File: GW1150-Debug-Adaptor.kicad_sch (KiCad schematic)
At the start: 5 parts, among them J1 SW_SPDT, J2 Conn_02x03_Counter_Clockwise, J3 Conn_02x03_Counter_Clockwise, J4 SW_SPDT, J5 Conn_01x06

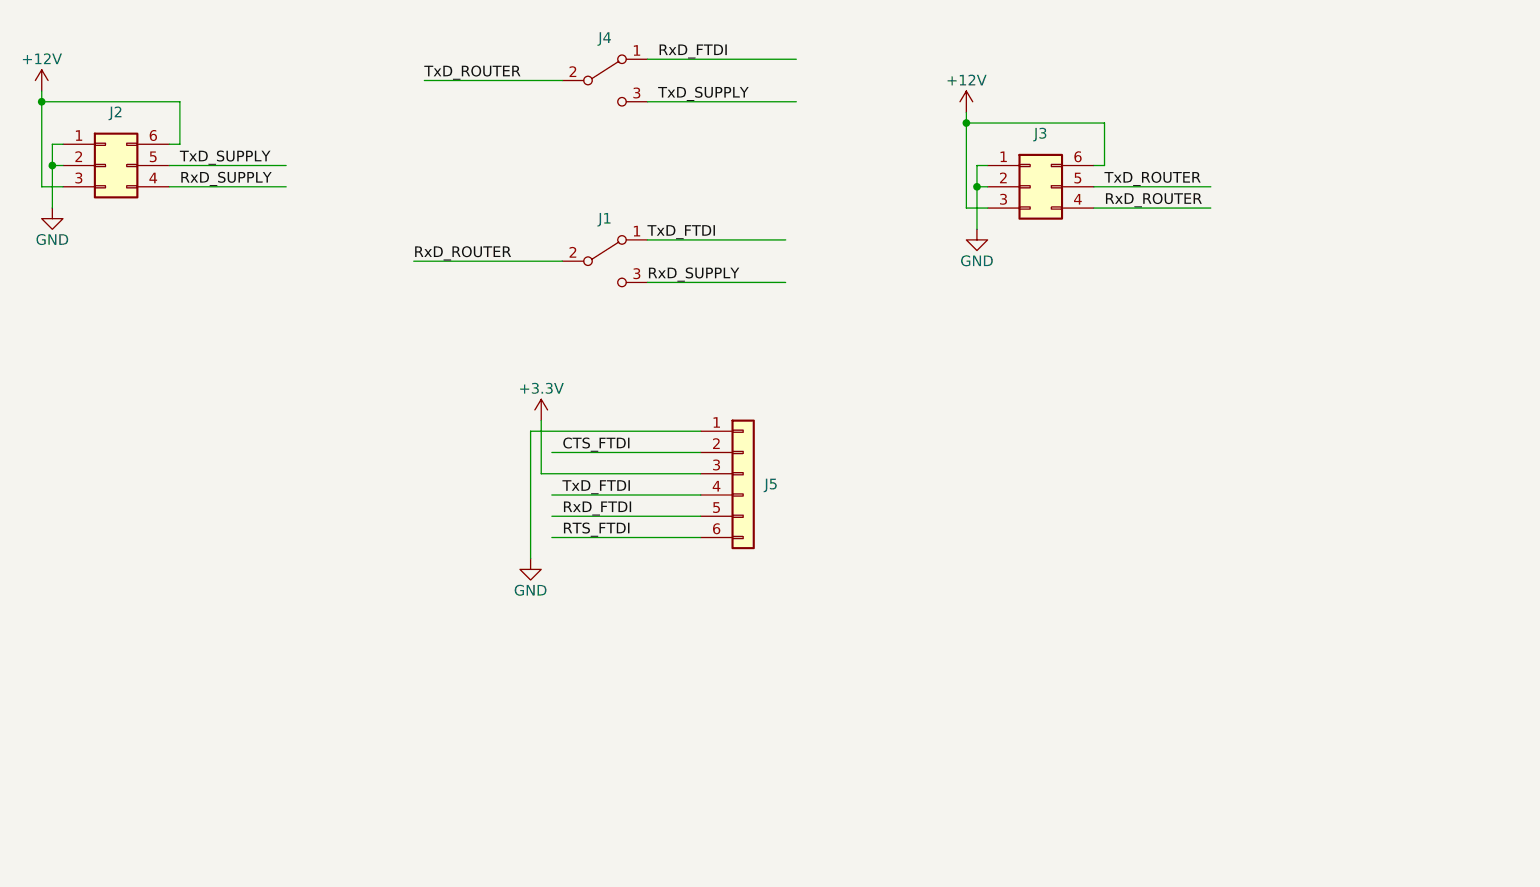
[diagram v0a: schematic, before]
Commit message: v1.0 changes after building initial units. Enlarged drill holes for cable whip. Added shunts across the jumpers, for default use. miscellaneous labeling.
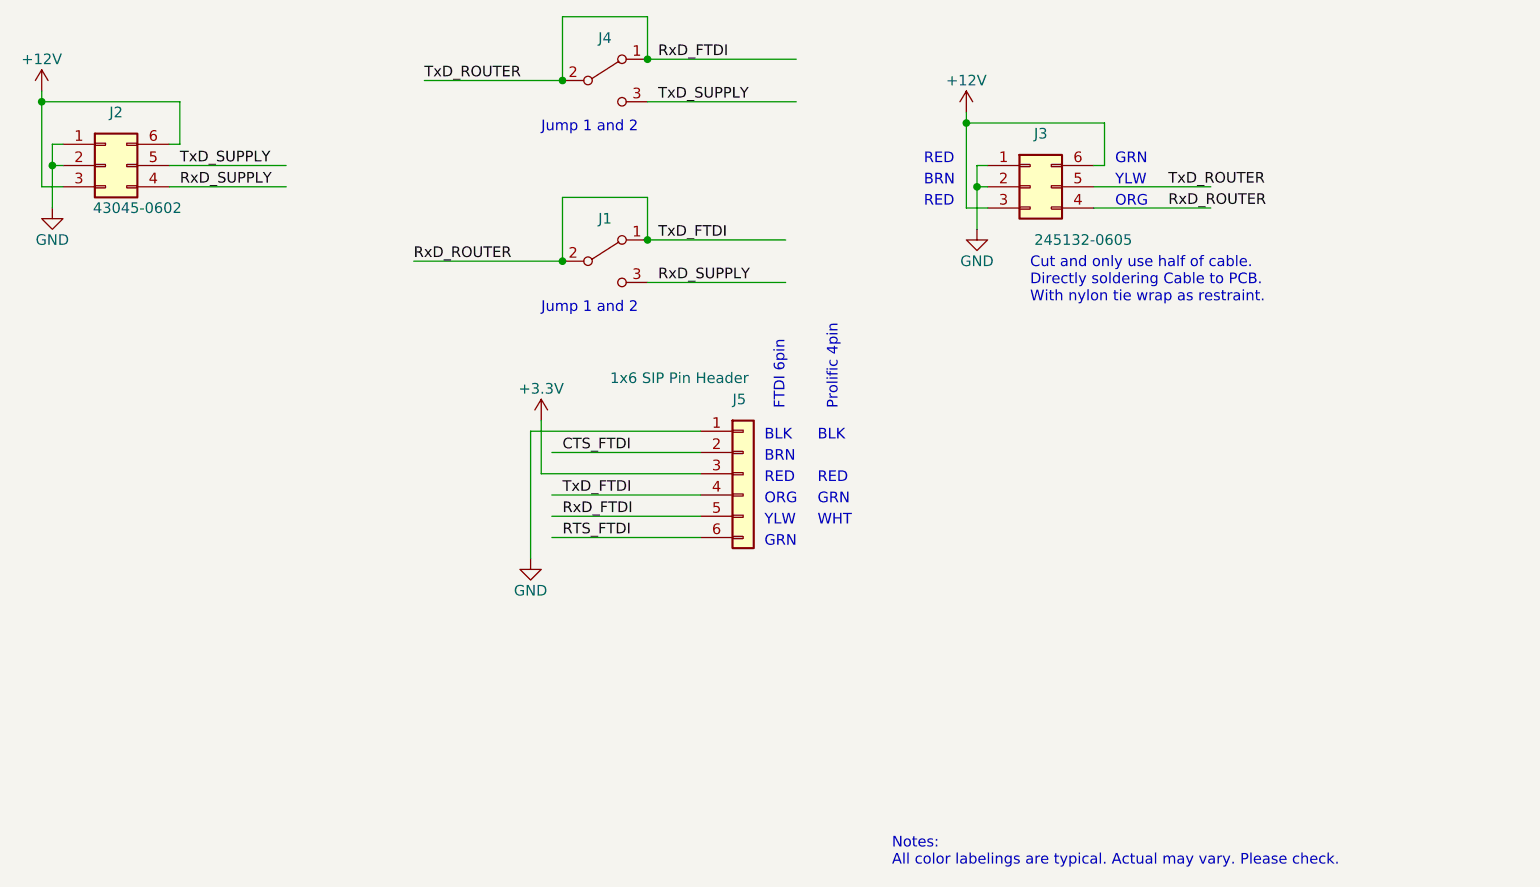
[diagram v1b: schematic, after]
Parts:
- J2: value Conn_02x03_Counter_Clockwise -> (none); footprint Connector_Molex:Molex_Micro-Fit_3.0_43045-0600_2x03_P3.00mm_Horizontal -> (none); MFGPN (none) -> 43045-0602
- J3: value Conn_02x03_Counter_Clockwise -> (none); footprint Connector_Molex:Molex_Micro-Fit_3.0_43045-0600_2x03_P3.00mm_Horizontal -> (none); MFGPN (none) -> 245132-0605
- J5: value Conn_01x06 -> (none); footprint Connector_PinSocket_2.54mm:PinSocket_1x06_P2.54mm_Vertical -> (none); MFGPN (none) -> 1x6 SIP Pin Header
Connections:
- net TxD_FTDI is gone; now on net RxD_ROUTER: J1.1 (A), J5.4 (Pin_4)
- net TxD_ROUTER is gone; now on net RxD_FTDI: J3.5 (Pin_5), J4.2 (B)
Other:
- note added: "BLK"
- note added: "BRN"
- note added: "Cut and only use half of cable. Directly soldering Cable to PCB. With nylon tie wrap as restraint."
- note added: "FTDI 6pin"
- note added: "GRN"
- note added: "Jump 1 and 2"
- note added: "Notes: All color labelings are typical. Actual may vary. Please check."
- note added: "ORG"
- note added: "Prolific 4pin"
- note added: "RED"
- note added: "WHT"
- note added: "YLW"
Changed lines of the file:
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@@
 (kicad_sch (version 20211123) (generator eeschema)
   (paper "A4")
+  (title_block
+    (date "2023-02-16")
+    (rev "1.0")
+  )
   (junction (at 80.01 86.36) (diameter 0) (color 0 0 0 0)
   )
   (junction (at 190.5 88.9) (diameter 0) (color 0 0 0 0)
   )
+  (junction (at 151.13 95.25) (diameter 0) (color 0 0 0 0)
+  )
   (junction (at 78.74 78.74) (diameter 0) (color 0 0 0 0)
   )
   (junction (at 189.23 81.28) (diameter 0) (color 0 0 0 0)
   )
+  (junction (at 151.13 73.66) (diameter 0) (color 0 0 0 0)
+  )
+  (junction (at 140.97 97.79) (diameter 0) (color 0 0 0 0)
+  )
+  (junction (at 140.97 76.2) (diameter 0) (color 0 0 0 0)
+  )
   (wire (pts (xy 205.74 86.36) (xy 205.74 81.28))
     (stroke (width 0) (type default) (color 0 0 0 0))
@@
     (stroke (width 0) (type default) (color 0 0 0 0))
   )
+  (wire (pts (xy 140.97 97.79) (xy 140.97 90.17))
+    (stroke (width 0) (type default) (color 0 0 0 0))
+  )
   (wire (pts (xy 157.48 118.11) (xy 137.16 118.11))
     (stroke (width 0) (type default) (color 0 0 0 0))
@@
     (stroke (width 0) (type default) (color 0 0 0 0))
   )
+  (wire (pts (xy 151.13 68.58) (xy 151.13 73.66))
+    (stroke (width 0) (type default) (color 0 0 0 0))
+  )
   (wire (pts (xy 204.47 88.9) (xy 218.44 88.9))
     (stroke (width 0) (type default) (color 0 0 0 0))
@@
     (stroke (width 0) (type default) (color 0 0 0 0))
   )
+  (wire (pts (xy 140.97 90.17) (xy 151.13 90.17))
+    (stroke (width 0) (type default) (color 0 0 0 0))
+  )
   (wire (pts (xy 151.13 95.25) (xy 167.64 95.25))
     (stroke (width 0) (type default) (color 0 0 0 0))
@@
     (stroke (width 0) (type default) (color 0 0 0 0))
   )
+  (wire (pts (xy 140.97 76.2) (xy 140.97 68.58))
+    (stroke (width 0) (type default) (color 0 0 0 0))
+  )
   (wire (pts (xy 81.28 88.9) (xy 78.74 88.9))
     (stroke (width 0) (type default) (color 0 0 0 0))
@@
     (stroke (width 0) (type default) (color 0 0 0 0))
   )
+  (wire (pts (xy 151.13 90.17) (xy 151.13 95.25))
+    (stroke (width 0) (type default) (color 0 0 0 0))
+  )
   (wire (pts (xy 139.7 120.65) (xy 157.48 120.65))
     (stroke (width 0) (type default) (color 0 0 0 0))
@@
     (stroke (width 0) (type default) (color 0 0 0 0))
   )
+  (wire (pts (xy 140.97 68.58) (xy 151.13 68.58))
+    (stroke (width 0) (type default) (color 0 0 0 0))
+  )
   (wire (pts (xy 204.47 86.36) (xy 205.74 86.36))
     (stroke (width 0) (type default) (color 0 0 0 0))
@@
     (stroke (width 0) (type default) (color 0 0 0 0))
   )
+  (text "WHT" (at 171.45 129.54 0)
+    (effects (font (size 1.27 1.27)) (justify left bottom))
+  )
+  (text "BRN" (at 184.15 88.9 0)
+    (effects (font (size 1.27 1.27)) (justify left bottom))
+  )
+  (text "Notes:\nAll color labelings are typical. Actual may vary. Please check."
+    (at 180.34 170.18 0)
+    (effects (font (size 1.27 1.27)) (justify left bottom))
+  )
+  (text "GRN" (at 207.01 86.36 0)
+    (effects (font (size 1.27 1.27)) (justify left bottom))
+  )
+  (text "Jump 1 and 2" (at 138.43 82.55 0)
+    (effects (font (size 1.27 1.27)) (justify left bottom))
+  )
+  (text "ORG" (at 207.01 91.44 0)
+    (effects (font (size 1.27 1.27)) (justify left bottom))
+  )
+  (text "RED" (at 184.15 91.44 0)
+    (effects (font (size 1.27 1.27)) (justify left bottom))
+  )
+  (text "RED" (at 171.45 124.46 0)
+    (effects (font (size 1.27 1.27)) (justify left bottom))
+  )
+  (text "FTDI 6pin" (at 167.64 115.57 90)
+    (effects (font (size 1.27 1.27)) (justify left bottom))
+  )
+  (text "Prolific 4pin" (at 173.99 115.57 90)
+    (effects (font (size 1.27 1.27)) (justify left bottom))
+  )
+  (text "Cut and only use half of cable.\nDirectly soldering Cable to PCB.\nWith nylon tie wrap as restraint."
+    (at 196.85 102.87 0)
+    (effects (font (size 1.27 1.27)) (justify left bottom))
+  )
+  (text "GRN" (at 165.1 132.08 0)
+    (effects (font (size 1.27 1.27)) (justify left bottom))
+  )
+  (text "RED" (at 184.15 86.36 0)
+    (effects (font (size 1.27 1.27)) (justify left bottom))
+  )
+  (text "ORG" (at 165.1 127 0)
+    (effects (font (size 1.27 1.27)) (justify left bottom))
+  )
+  (text "GRN" (at 171.45 127 0)
+    (effects (font (size 1.27 1.27)) (justify left bottom))
+  )
+  (text "Jump 1 and 2" (at 138.43 104.14 0)
+    (effects (font (size 1.27 1.27)) (justify left bottom))
+  )
+  (text "BLK" (at 171.45 119.38 0)
+    (effects (font (size 1.27 1.27)) (justify left bottom))
+  )
+  (text "YLW" (at 207.01 88.9 0)
+    (effects (font (size 1.27 1.27)) (justify left bottom))
+  )
+  (text "BRN" (at 165.1 121.92 0)
+    (effects (font (size 1.27 1.27)) (justify left bottom))
+  )
+  (text "BLK" (at 165.1 119.38 0)
+    (effects (font (size 1.27 1.27)) (justify left bottom))
+  )
+  (text "YLW" (at 165.1 129.54 0)
+    (effects (font (size 1.27 1.27)) (justify left bottom))
+  )
+  (text "RED" (at 165.1 124.46 0)
+    (effects (font (size 1.27 1.27)) (justify left bottom))
+  )
   (label "TxD_ROUTER" (at 124.46 76.2 0)
     (effects (font (size 1.27 1.27)) (justify left bottom))
@@
     (effects (font (size 1.27 1.27)) (justify left bottom))
   )
-  (label "TxD_FTDI" (at 151.13 95.25 0)
+  (label "TxD_FTDI" (at 152.4 95.25 0)
     (effects (font (size 1.27 1.27)) (justify left bottom))
   )
@@
     (effects (font (size 1.27 1.27)) (justify left bottom))
   )
-  (label "RxD_SUPPLY" (at 151.13 100.33 0)
-    (effects (font (size 1.27 1.27)) (justify left bottom))
-  )
-  (label "TxD_ROUTER" (at 205.74 88.9 0)
-    (effects (font (size 1.27 1.27)) (justify left bottom))
-  )
-  (label "RxD_ROUTER" (at 205.74 91.44 0)
+  (label "RxD_SUPPLY" (at 152.4 100.33 0)
+    (effects (font (size 1.27 1.27)) (justify left bottom))
+  )
+  (label "TxD_ROUTER" (at 213.36 88.9 0)
+    (effects (font (size 1.27 1.27)) (justify left bottom))
+  )
+  (label "RxD_ROUTER" (at 213.36 91.44 0)
     (effects (font (size 1.27 1.27)) (justify left bottom))
   )
@@
   )
   (symbol (lib_id "Connector_Generic:Conn_02x03_Counter_Clockwise") (at 86.36 86.36 0) (unit 1)
-    (in_bom yes) (on_board yes) (fields_autoplaced)
+    (in_bom yes) (on_board yes)
     (property "Reference" "J2" (id 0) (at 87.63 80.01 0))
-    (property "Value" "Conn_02x03_Counter_Clockwise" (id 1) (at 87.63 80.01 0)
-      (effects (font (size 1.27 1.27)) hide)
-    )
-    (property "Footprint" "Connector_Molex:Molex_Micro-Fit_3.0_43045-0600_2x03_P3.00mm_Horizontal" (id 2) (at 86.36 86.36 0)
+    (property "Value" "" (id 1) (at 87.63 80.01 0)
+      (effects (font (size 1.27 1.27)) hide)
+    )
+    (property "Footprint" "" (id 2) (at 86.36 86.36 0)
       (effects (font (size 1.27 1.27)) hide)
     )
@@
       (effects (font (size 1.27 1.27)) hide)
     )
+    (property "MFGPN" "43045-0602" (id 4) (at 90.17 91.44 0))
     (pin "1")
     (pin "2")
@@
   )
   (symbol (lib_id "Connector_Generic:Conn_01x06") (at 162.56 123.19 0) (unit 1)
-    (in_bom yes) (on_board yes) (fields_autoplaced)
-    (property "Reference" "J5" (id 0) (at 165.1 124.4599 0)
+    (in_bom yes) (on_board yes)
+    (property "Reference" "J5" (id 0) (at 161.29 114.3 0)
       (effects (font (size 1.27 1.27)) (justify left))
     )
-    (property "Value" "Conn_01x06" (id 1) (at 165.1 125.7299 0)
+    (property "Value" "" (id 1) (at 165.1 125.7299 0)
       (effects (font (size 1.27 1.27)) (justify left) hide)
     )
-    (property "Footprint" "Connector_PinSocket_2.54mm:PinSocket_1x06_P2.54mm_Vertical" (id 2) (at 162.56 123.19 0)
+    (property "Footprint" "" (id 2) (at 162.56 123.19 0)
       (effects (font (size 1.27 1.27)) hide)
     )
@@
       (effects (font (size 1.27 1.27)) hide)
     )
+    (property "MFGPN" "1x6 SIP Pin Header" (id 4) (at 154.94 111.76 0))
     (pin "1")
     (pin "2")
@@
   )
   (symbol (lib_id "Connector_Generic:Conn_02x03_Counter_Clockwise") (at 196.85 88.9 0) (unit 1)
-    (in_bom yes) (on_board yes) (fields_autoplaced)
+    (in_bom yes) (on_board yes)
     (property "Reference" "J3" (id 0) (at 198.12 82.55 0))
-    (property "Value" "Conn_02x03_Counter_Clockwise" (id 1) (at 198.12 82.55 0)
-      (effects (font (size 1.27 1.27)) hide)
-    )
-    (property "Footprint" "Connector_Molex:Molex_Micro-Fit_3.0_43045-0600_2x03_P3.00mm_Horizontal" (id 2) (at 196.85 88.9 0)
+    (property "Value" "" (id 1) (at 198.12 82.55 0)
+      (effects (font (size 1.27 1.27)) hide)
+    )
+    (property "Footprint" "" (id 2) (at 196.85 88.9 0)
       (effects (font (size 1.27 1.27)) hide)
     )
@@
       (effects (font (size 1.27 1.27)) hide)
     )
+    (property "MFGPN" "245132-0605" (id 4) (at 203.2 95.25 0))
     (pin "1")
     (pin "2")
